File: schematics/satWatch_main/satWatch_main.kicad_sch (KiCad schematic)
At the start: 120 parts, among them J1 PogoPins_02x17_Data, J2 UJ20-C-H-G-MSMT-2B-P16-TR, J5 Pogo_02x03_Power, Q1 FS8205, Q2 BSS138, Q3 DMP1045U, Q4 BSS138, SW1 B3U-1000P, SW2 B3U-1000P, SW3 B3U-1000P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

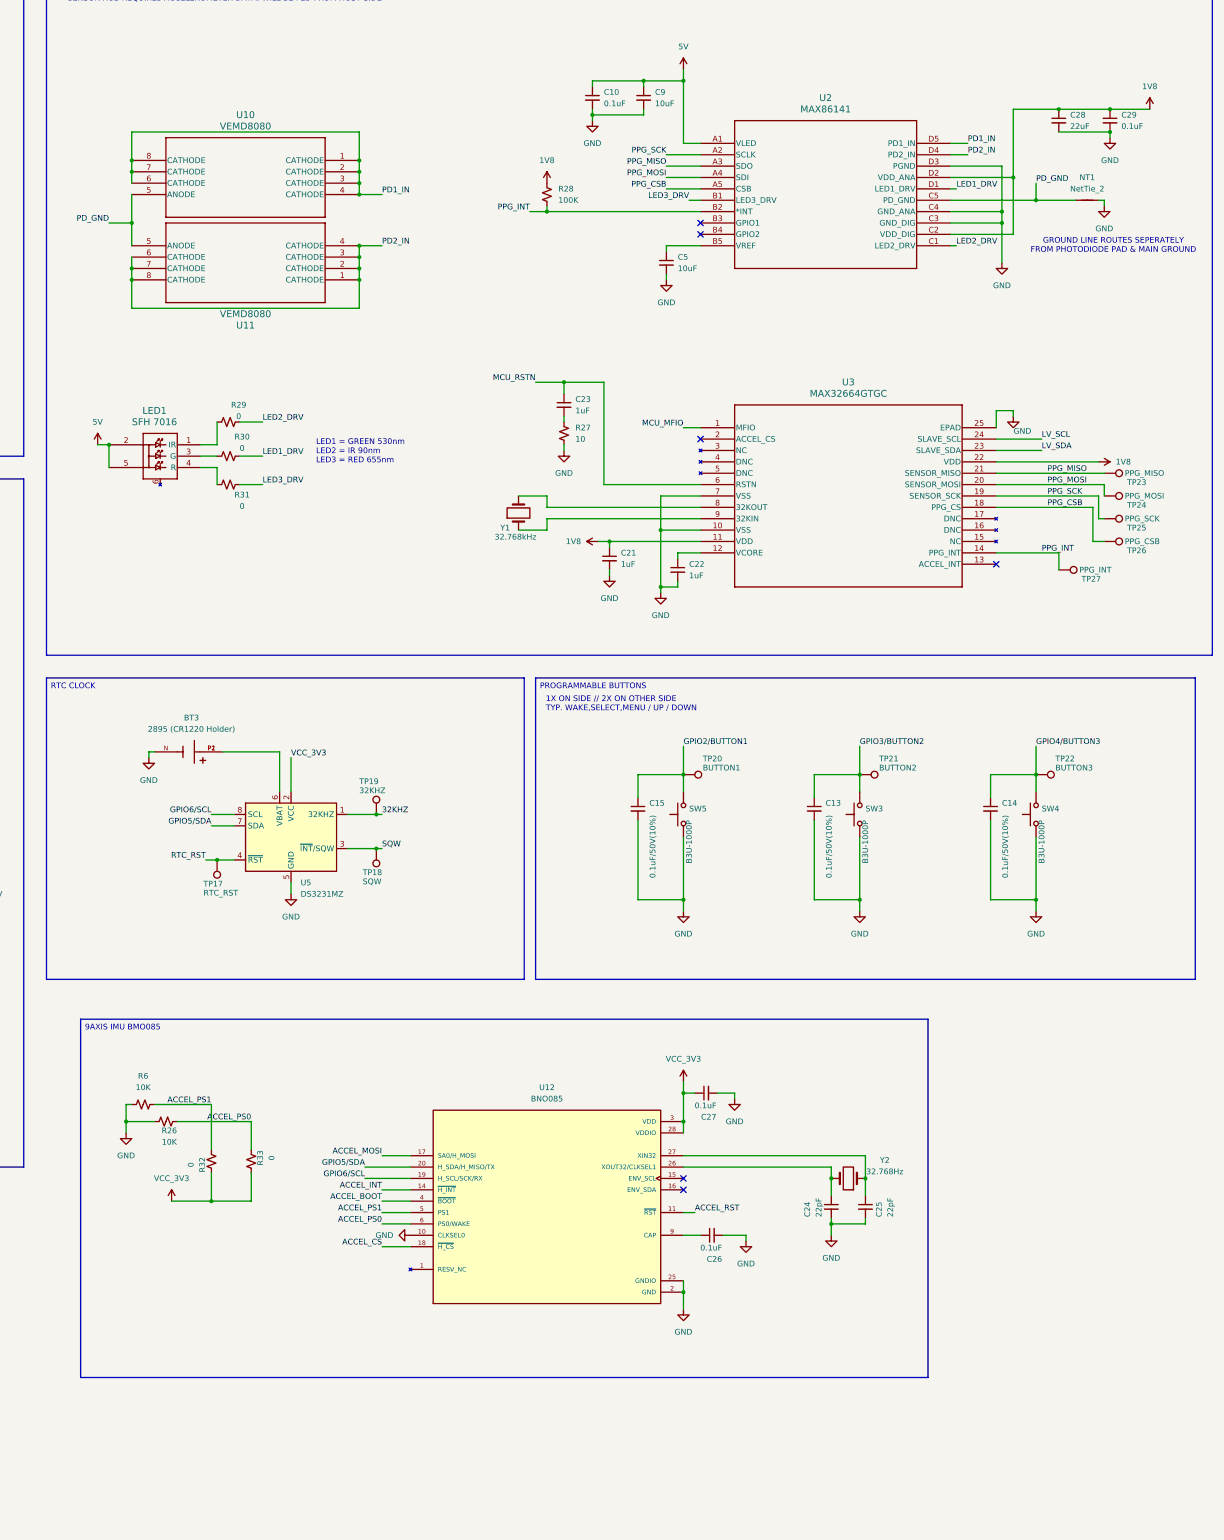
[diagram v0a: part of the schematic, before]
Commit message: v0.4
Finalized large prototyping PCB for manufacturing
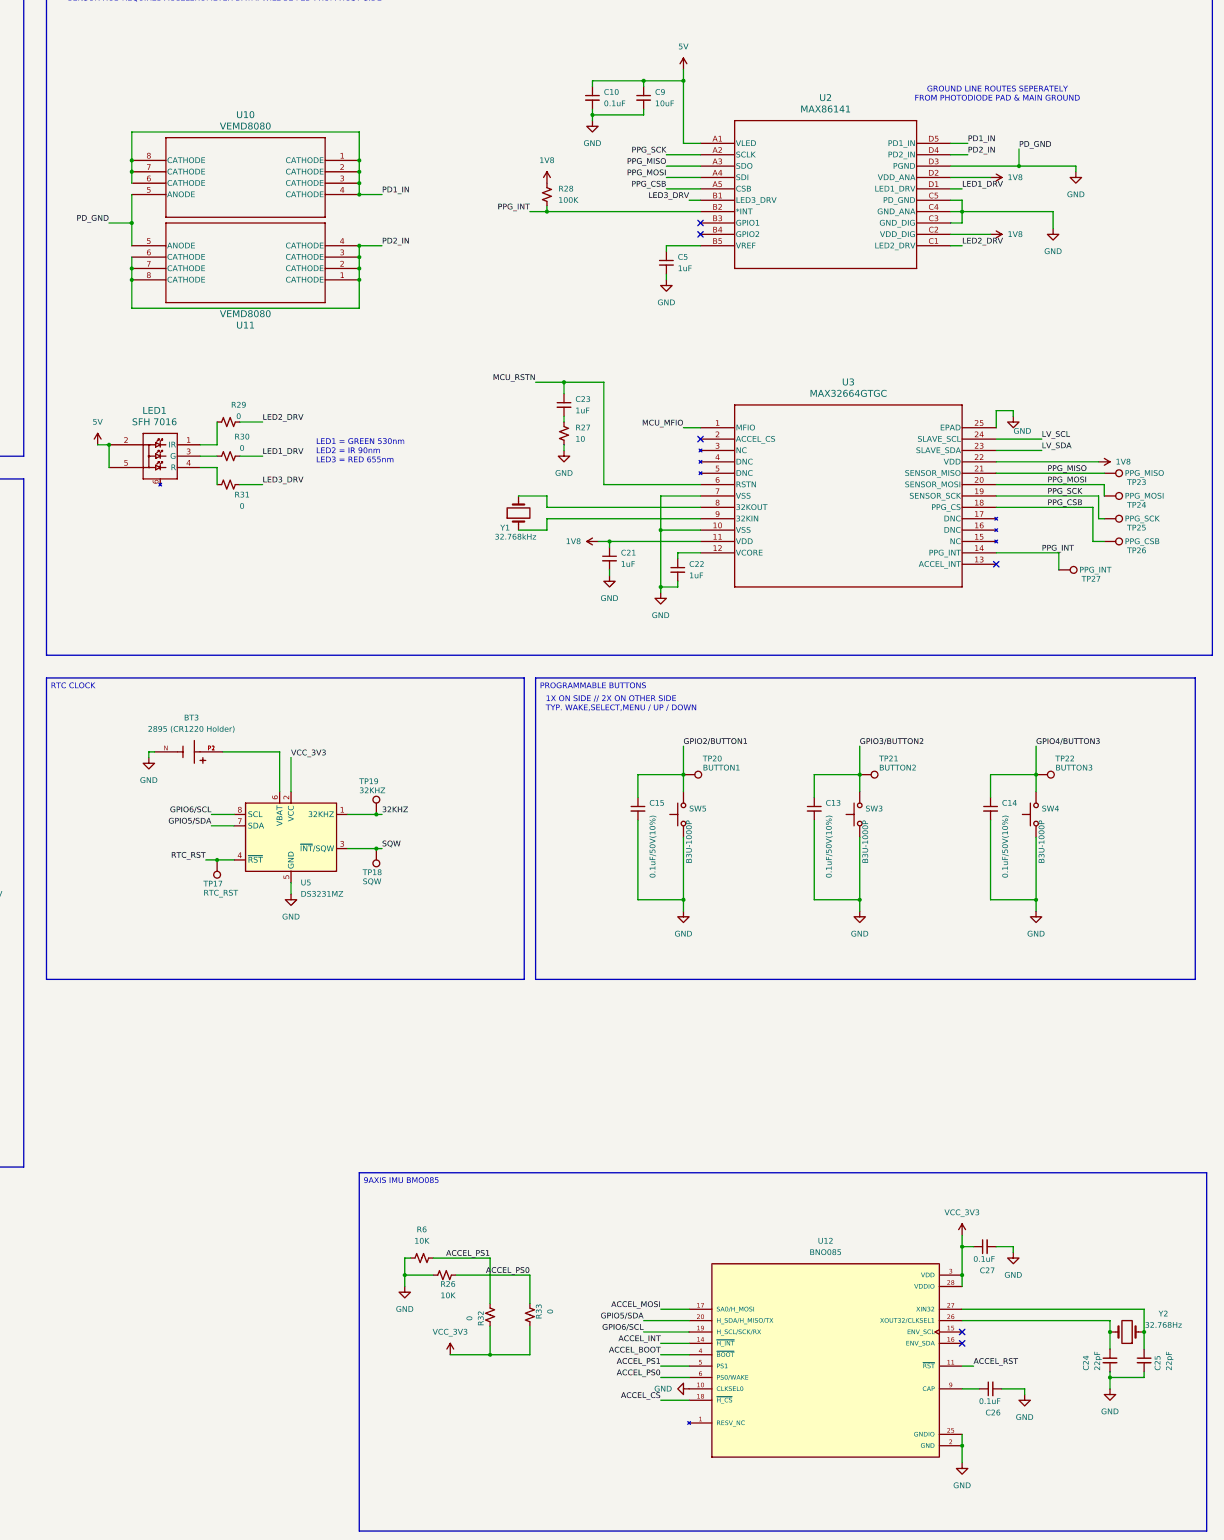
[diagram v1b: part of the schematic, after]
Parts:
- removed C28: 22uF, Capacitor_SMD:C_0603_1608Metric_Pad1.08x0.95mm_HandSolder, symbol Device:C_Small
- removed C29: 0.1uF, Capacitor_SMD:C_0603_1608Metric_Pad1.08x0.95mm_HandSolder, symbol Device:C_Small
- removed NT1: NetTie_2, NetTie:NetTie-2_SMD_Pad0.5mm, symbol Device:NetTie_2
- C5: value 10uF -> 1uF
- U1: footprint footprint:ESP32-S2-MINI-1 -> RF_Module:ESP32-S2-MINI-1
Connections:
- net PD_GND is gone; now on net GND: U10.5 (ANODE), U11.5 (ANODE), U2.C5 (PD_GND)
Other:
- title: MAINBOARD: LARGE PROTOTYPE -> MAINBOARD
- moved on the sheet: C24, C25, C26, C27, R26, R32, R33, R6, U12, Y2
